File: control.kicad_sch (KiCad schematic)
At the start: 22 parts, among them J7 Conn_01x06_Male, J9 Conn_02x15_Odd_Even, SW2 SW_Push, U1 MX6UL-VM, U28 74LVC1G123, Y1 24Mhz, Y2 32.768kHz

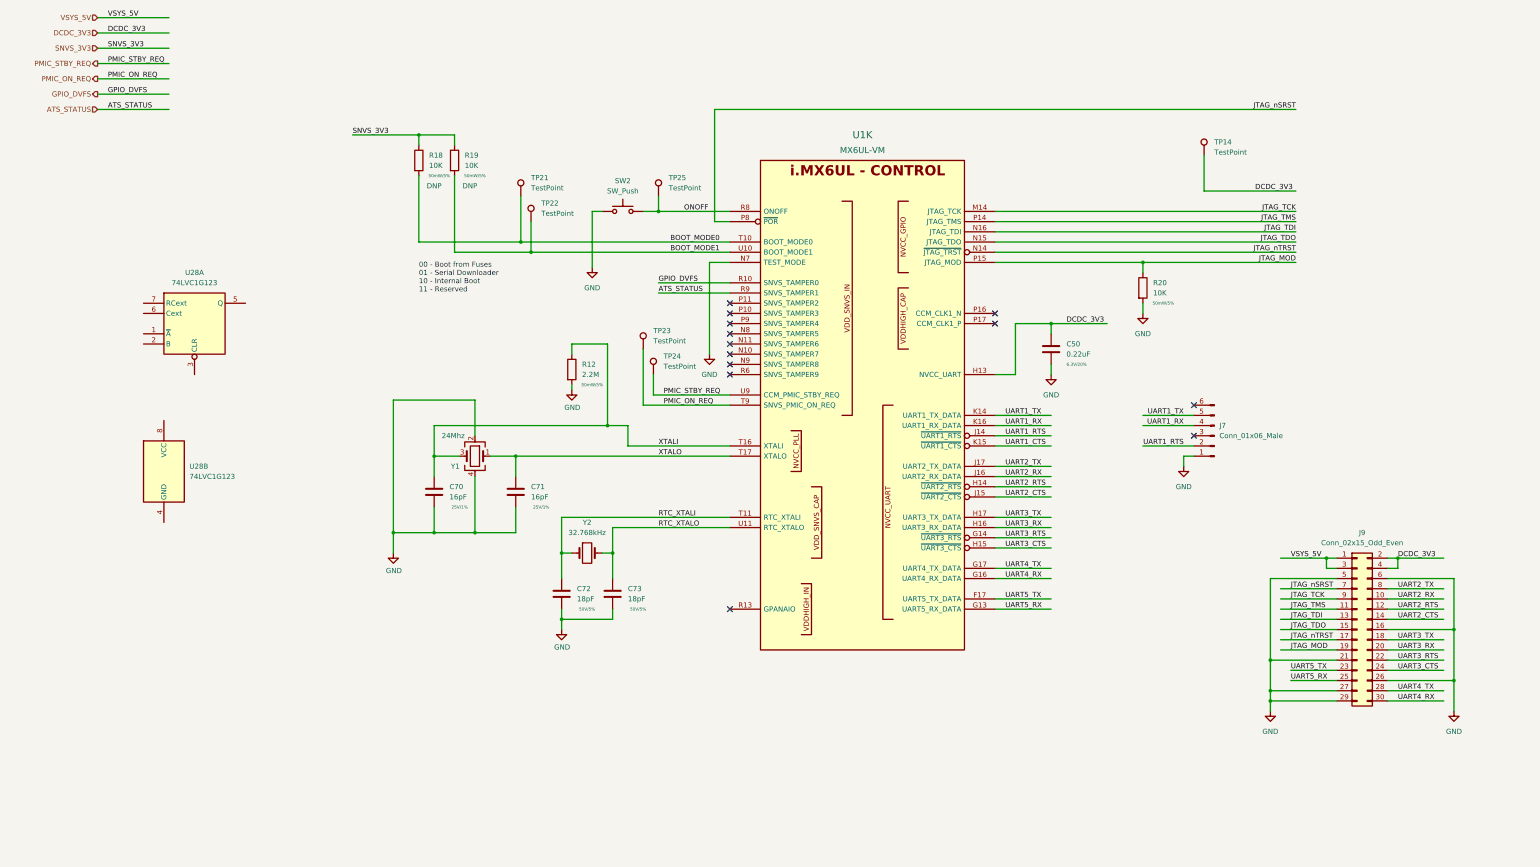
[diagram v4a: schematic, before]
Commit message: lots of routing, ddr length matching done
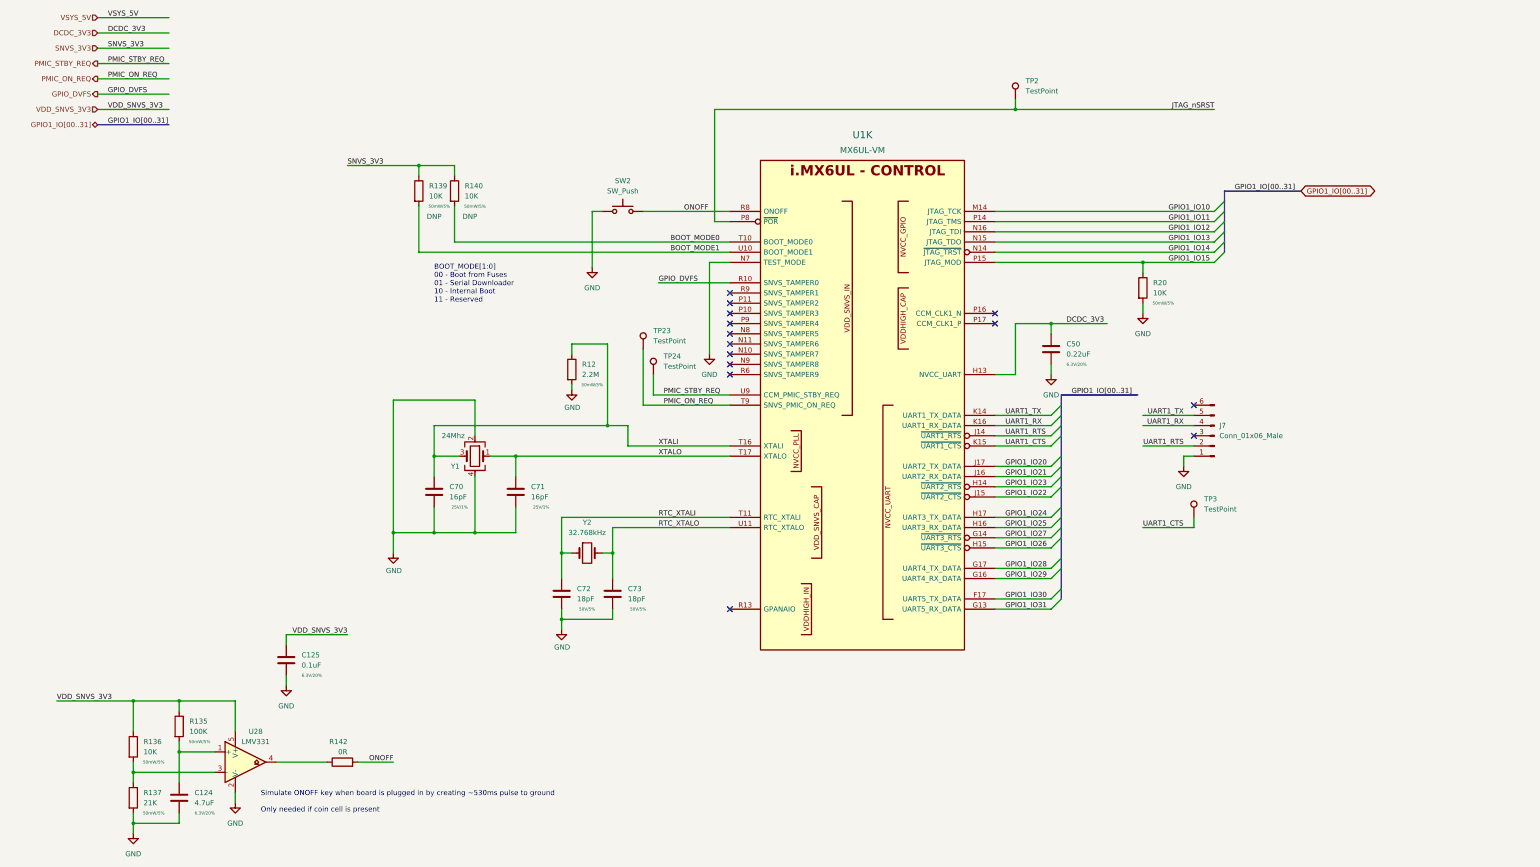
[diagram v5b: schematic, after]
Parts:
- removed J9: Conn_02x15_Odd_Even, Connector_PinHeader_2.54mm:PinHeader_2x15_P2.54mm_Vertical_SMD, symbol Connector_Generic:Conn_02x15_Odd_Even
- removed R18, R19: 10K, Resistor_SMD:R_0402_1005Metric, symbol Device:R
- removed TP14, TP21, TP22, TP25: TestPoint, TestPoint:TestPoint_Pad_D1.0mm, symbol Connector:TestPoint
- removed U28: 74LVC1G123, imx6ull-sbc:SOT1203, symbol 74xGxx:74LVC1G123
- added C124: 4.7uF, Capacitor_SMD:C_0402_1005Metric, symbol Device:C
- added C125: 0.1uF, Capacitor_SMD:C_0402_1005Metric, symbol Device:C
- added R135: 100K, Resistor_SMD:R_0402_1005Metric, symbol Device:R
- added R136, R139, R140: 10K, Resistor_SMD:R_0402_1005Metric, symbol Device:R
- added R137: 21K, Resistor_SMD:R_0402_1005Metric, symbol Device:R
- added R142: 0R, Resistor_SMD:R_0402_1005Metric, symbol Device:R
- added TP2, TP3: TestPoint, TestPoint:TestPoint_Pad_D1.0mm, symbol Connector:TestPoint
- added U28: LMV331, Package_TO_SOT_SMD:SOT-23-5, symbol Comparator:LMV331
- U1: footprint imx6ull-sbc:SOT1534-2 -> qsbc-zero:SOT1534-2; symbol imx6ull-sbc:MX6UL-VM -> qsbc-zero:MX6UL-VM
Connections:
- net BOOT_MODE0: now also R140.2
- net BOOT_MODE1: now also R139.2
- net GND: now also C124.2, C125.2, R137.2, U28.2 (V-)
- net JTAG_nSRST: now also TP2.1
- net ONOFF: now also R142.2
- net SNVS_3V3: now also R139.1, R140.1
- net UART1_CTS: now also TP3.1
- net ATS_STATUS: no longer names the net of U1.R9 (SNVS_TAMPER1)
- net JTAG_MOD renamed GPIO1_IO15
- net JTAG_TCK renamed GPIO1_IO10
- net JTAG_TDI renamed GPIO1_IO12
- net JTAG_TDO renamed GPIO1_IO13
- net JTAG_TMS renamed GPIO1_IO11
- net JTAG_nTRST renamed GPIO1_IO14
- net UART2_CTS renamed GPIO1_IO22
- net UART2_RTS renamed GPIO1_IO23
- net UART2_RX renamed GPIO1_IO21
- net UART2_TX renamed GPIO1_IO20
- net UART3_CTS renamed GPIO1_IO26
- net UART3_RTS renamed GPIO1_IO27
- net UART3_RX renamed GPIO1_IO25
- net UART3_TX renamed GPIO1_IO24
- net UART4_RX renamed GPIO1_IO29
- net UART4_TX renamed GPIO1_IO28
- net UART5_RX renamed GPIO1_IO31
- net UART5_TX renamed GPIO1_IO30
- new net: R142.1, U28.4
- new net: C124.1, R135.2, U28.1 (+)
- new net: R136.2, R137.1, U28.3 (-)
- new net VDD_SNVS_3V3: C125.1, R135.1, R136.1, U28.5 (V+)
- no-connect marks 13 -> 14
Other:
- note added: "BOOT_MODE[1:0] 00 - Boot from Fuses 01 - Serial Downloader 10 - Internal Boot 11 - Reserved"
- note added: "Simulate ONOFF key when board is plugged in by creating ~530ms pulse to ground Only needed if coin cell is present"
- note removed: "00 - Boot from Fuses 01 - Serial Downloader 10 - Internal Boot 11 - Reserved"

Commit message: more pcb work, bom work
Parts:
- added JP1, JP2: Jumper_2_Open, Jumper:SolderJumper-2_P1.3mm_Open_RoundedPad1.0x1.5mm, symbol Jumper:Jumper_2_Open
- added TP4: TestPoint, TestPoint:TestPoint_Pad_D1.0mm, symbol Connector:TestPoint
- C124: DigiKey_PN (none) -> 1276-1482-1-ND; MPN (none) -> CL05A475MP5NRNC; Rating 6.3V/20% -> 10V/20%
- C125: DigiKey_PN (none) -> 490-14603-1-ND; MPN (none) -> GRM155R71E104KE14J; Rating 6.3V/20% -> 25V/20%
- C50: DigiKey_PN (none) -> 490-10392-1-ND; MPN (none) -> GRM033C80J224KE90D
- C70, C71: DigiKey_PN (none) -> 490-GCM1555C1H160JA16DCT-ND; MPN (none) -> GCM1555C1H160JA16D; Rating 25V/1% -> 50V/1%
- C72, C73: DigiKey_PN (none) -> 311-1415-1-ND; MPN (none) -> CC0402JRNPO9BN180
- J7: DigiKey_PN (none) -> 952-3267-ND; MPN (none) -> M20-8900605
- R12: DigiKey_PN (none) -> 13-RC0402FR-132M2LCT-ND; MPN (none) -> RC0402FR-132M2L; Rating 50mW/5% -> 50mW/1%
- R135: DigiKey_PN (none) -> CR0402-FX-1003GLFCT-ND; MPN (none) -> CR0402-FX-1003GLF; Rating 50mW/5% -> 50mW/1%
- R136, R20: DigiKey_PN (none) -> 311-10KJRCT-ND; MPN (none) -> RC0402JR-0710KL
- R137: DigiKey_PN (none) -> 311-21.0KLRCT-ND; MPN (none) -> RC0402FR-0721KL
- R139, R140: DNP DNP -> (none); DigiKey_PN (none) -> 311-10KJRCT-ND; MPN (none) -> RC0402JR-0710KL
- R142: DigiKey_PN (none) -> 311-0.0LRCT-ND; MPN (none) -> RC0402FR-070RL
- SW2: DigiKey_PN (none) -> CKN9120-ND; MPN (none) -> PTS645VH58-2 LFS
- U1: DigiKey_PN (none) -> 568-14995-ND; MPN (none) -> MCIMX6Y2DVM09AB
- U28: DigiKey_PN (none) -> LMV331M5X/NOPBCT-ND; MPN (none) -> LMV331M5X/NOPB
- Y1: DigiKey_PN (none) -> XC2477CT-ND; MPN Q 24,0-JXS32-9-10/15-T1-FU-WA-LF -> ECS-240-9-33B-CWN-TR
- Y2: DigiKey_PN (none) -> 300-8816-1-ND; MPN FC-135 32.7680KA-A0 -> CM315D32768EZFT
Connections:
- net BOOT_MODE0: now also JP2.1 (A); no longer R140.2
- net BOOT_MODE1: now also JP1.1 (A); no longer R139.2
- net GPIO_DVFS: now also TP4.1
- new net: JP1.2 (B), R139.2
- new net: JP2.2 (B), R140.2
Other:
- moved on the sheet: R139, R140

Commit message: add basic readme, rev 1 of pcb
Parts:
- removed C124: 4.7uF, Capacitor_SMD:C_0402_1005Metric, symbol Device:C
- removed C125: 0.1uF, Capacitor_SMD:C_0402_1005Metric, symbol Device:C
- removed R135: 100K, Resistor_SMD:R_0402_1005Metric, symbol Device:R
- removed R136: 10K, Resistor_SMD:R_0402_1005Metric, symbol Device:R
- removed R137: 21K, Resistor_SMD:R_0402_1005Metric, symbol Device:R
- removed R142: 0R, Resistor_SMD:R_0402_1005Metric, symbol Device:R
- removed SW2: SW_Push, Button_Switch_THT:SW_Tactile_SPST_Angled_PTS645Vx58-2LFS, symbol Switch:SW_Push
- removed TP2, TP23, TP24, TP4: TestPoint, TestPoint:TestPoint_Pad_D1.0mm, symbol Connector:TestPoint
- removed U28: LMV331, Package_TO_SOT_SMD:SOT-23-5, symbol Comparator:LMV331
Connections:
- net GPIO_DVFS renamed ~{PMIC_INT}
- net JTAG_nSRST renamed ~{POR}
- net SNVS_3V3 renamed SNVS_3V
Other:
- note removed: "Simulate ONOFF key when board is plugged in by creating ~530ms pulse to ground Only needed if coin cell is present"
